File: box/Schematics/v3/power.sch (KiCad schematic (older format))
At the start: 28 parts, among them U1 AMC1100DWV, U2 ADUM5010ARSZ

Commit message: finish dsp schematics
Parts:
- added C12, C13: C, symbol C
- added U3: ISL21010CFH333Z-TK, symbol ISL21010CFH333Z-TK
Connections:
- net labels added: 3.3VREF, ADC, IN+, IN-
- net labels removed: ADC_IN+, ADC_IN-
- wire segments 97 -> 105

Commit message: create connectors sheet
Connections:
- net labels added: ADC_IN+, ADC_IN-
- net labels removed: ADC, IN+, IN-
- wire segments 105 -> 104
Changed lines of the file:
@@
 LIBS:power
 LIBS:conn
-LIBS:contrib
-LIBS:stm32
 LIBS:opqbox3-cache
 EELAYER 25 0
@@
 $Descr A4 11693 8268
 encoding utf-8
-Sheet 2 3
+Sheet 2 4
 Title ""
 Date ""
@@
 Text HLabel 1700 1950 0    60   Input ~ 0
 NEUTRAL
-Text HLabel 8500 1450 2    60   Output ~ 0
-+3.3V
-Text HLabel 5350 1350 2    60   Output ~ 0
-+5V
-Text HLabel 5350 1750 2    60   Output ~ 0
-GND
 $Comp
 L PWR_FLAG #FLG021
 U 1 1 5A83249D
-P 5200 1800
-F 0 "#FLG021" H 5200 1875 50  0001 C CNN
-F 1 "PWR_FLAG" H 5200 1950 50  0000 C CNN
-F 2 "" H 5200 1800 50  0001 C CNN
-F 3 "" H 5200 1800 50  0001 C CNN
-	1    5200 1800
+P 4900 1850
+F 0 "#FLG021" H 4900 1925 50  0001 C CNN
+F 1 "PWR_FLAG" H 4900 2000 50  0000 C CNN
+F 2 "" H 4900 1850 50  0001 C CNN
+F 3 "" H 4900 1850 50  0001 C CNN
+	1    4900 1850
 	-1   0    0    1
 $EndComp
@@
 	8400 1200 8400 1600
 Wire Wire Line
-	8200 1450 8500 1450
-Wire Wire Line
 	6800 1900 6800 2250
 Wire Wire Line
@@
 	8400 2250 8400 1900
 Connection ~ 6800 1450
-Connection ~ 8400 1450
 Wire Wire Line
 	2600 1050 2600 1500
@@
 	4300 1700 4300 1850
 Wire Wire Line
-	4900 1750 4900 1700
+	4900 1700 4900 1850
 Wire Wire Line
 	7000 1450 6800 1450
@@
 Connection ~ 4900 4200
 Connection ~ 4900 3900
-Wire Wire Line
-	4800 3900 5150 3900
-Wire Wire Line
-	4800 4200 5150 4200
 Connection ~ 5200 1350
 Wire Wire Line
@@
 Wire Notes Line
 	3600 7800 3600 500
-Wire Wire Line
-	4000 1750 5350 1750
 Connection ~ 4300 1750
 Wire Wire Line
 	4100 1350 4450 1350
-Wire Wire Line
-	4750 1350 5350 1350
 Connection ~ 4900 1750
-Connection ~ 5200 1750
-Wire Wire Line
-	5200 1800 5200 1750
 Wire Wire Line
 	5200 1350 5200 1300
@@
 	1    0    0    -1
 $EndComp
-Entry Wire Line
-	5150 3900 5250 4000
-Entry Wire Line
-	5150 4200 5250 4300
-Text Label 5050 3900 0    60   ~ 0
-IN+
-Text Label 5050 4200 0    60   ~ 0
-IN-
-Wire Bus Line
-	5250 4000 5250 4350
-Wire Bus Line
-	5250 4350 5400 4350
-Text HLabel 5400 4350 2    60   Output ~ 0
-ADC
+Text HLabel 5100 4200 2    60   Output ~ 0
+ADC_IN-
+Text HLabel 5100 3900 2    60   Output ~ 0
+ADC_IN+
+Wire Wire Line
+	4800 4200 5100 4200
+Wire Wire Line
+	4800 3900 5100 3900
+Wire Wire Line
+	4750 1350 5200 1350
+Wire Wire Line
+	4000 1750 4900 1750
+Wire Wire Line
+	8200 1450 8400 1450
+Connection ~ 8400 1450
 $EndSCHEMATC

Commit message: add component values
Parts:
- C1, C13, C2, C5, C6, C8: value C -> 0.1uF
- C10, C11: value CP -> 1uF
- C12: value C -> 1uF
- C3, C9: value C -> 10uF
- C4, C7: value CP -> 22uF
- R1: value R -> 990k
- R2: value R -> 1k
- R3, R4, R8, R9: value R -> 66.5
- R5: value R -> 30.9k
- R6, R7: value R -> 10k
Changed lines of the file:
@@
 P 6800 1750
 F 0 "C10" H 6825 1850 50  0000 L CNN
-F 1 "CP" H 6825 1650 50  0000 L CNN
+F 1 "1uF" H 6825 1650 50  0000 L CNN
 F 2 "" H 6838 1600 50  0001 C CNN
 F 3 "" H 6800 1750 50  0001 C CNN
@@
 P 8400 1750
 F 0 "C11" H 8425 1850 50  0000 L CNN
-F 1 "CP" H 8425 1650 50  0000 L CNN
+F 1 "1uF" H 8425 1650 50  0000 L CNN
 F 2 "" H 8438 1600 50  0001 C CNN
 F 3 "" H 8400 1750 50  0001 C CNN
@@
 P 4300 1550
 F 0 "C4" H 4325 1650 50  0000 L CNN
-F 1 "CP" H 4325 1450 50  0000 L CNN
+F 1 "22uF" H 4325 1450 50  0000 L CNN
 F 2 "" H 4338 1400 50  0001 C CNN
 F 3 "" H 4300 1550 50  0001 C CNN
@@
 P 4900 1550
 F 0 "C7" H 4925 1650 50  0000 L CNN
-F 1 "CP" H 4925 1450 50  0000 L CNN
+F 1 "22uF" H 4925 1450 50  0000 L CNN
 F 2 "" H 4938 1400 50  0001 C CNN
 F 3 "" H 4900 1550 50  0001 C CNN
@@
 P 2150 3600
 F 0 "R1" V 2230 3600 50  0000 C CNN
-F 1 "R" V 2150 3600 50  0000 C CNN
+F 1 "990k" V 2150 3600 50  0000 C CNN
 F 2 "" V 2080 3600 50  0001 C CNN
 F 3 "" H 2150 3600 50  0001 C CNN
@@
 P 2150 4150
 F 0 "R2" V 2230 4150 50  0000 C CNN
-F 1 "R" V 2150 4150 50  0000 C CNN
+F 1 "1k" V 2150 4150 50  0000 C CNN
 F 2 "" V 2080 4150 50  0001 C CNN
 F 3 "" H 2150 4150 50  0001 C CNN
@@
 P 2400 3900
 F 0 "R3" V 2480 3900 50  0000 C CNN
-F 1 "R" V 2400 3900 50  0000 C CNN
+F 1 "66.5" V 2400 3900 50  0000 C CNN
 F 2 "" V 2330 3900 50  0001 C CNN
 F 3 "" H 2400 3900 50  0001 C CNN
@@
 P 2400 4400
 F 0 "R4" V 2480 4400 50  0000 C CNN
-F 1 "R" V 2400 4400 50  0000 C CNN
+F 1 "66.5" V 2400 4400 50  0000 C CNN
 F 2 "" V 2330 4400 50  0001 C CNN
 F 3 "" H 2400 4400 50  0001 C CNN
@@
 P 2650 4150
 F 0 "C2" H 2675 4250 50  0000 L CNN
-F 1 "C" H 2675 4050 50  0000 L CNN
+F 1 "0.1uF" H 2675 4050 50  0000 L CNN
 F 2 "" H 2688 4000 50  0001 C CNN
 F 3 "" H 2650 4150 50  0001 C CNN
@@
 P 2650 3300
 F 0 "C1" H 2675 3400 50  0000 L CNN
-F 1 "C" H 2675 3200 50  0000 L CNN
+F 1 "0.1uF" H 2675 3200 50  0000 L CNN
 F 2 "" H 2688 3150 50  0001 C CNN
 F 3 "" H 2650 3300 50  0001 C CNN
@@
 P 3050 5550
 F 0 "C3" H 3075 5650 50  0000 L CNN
-F 1 "C" H 3075 5450 50  0000 L CNN
+F 1 "10uF" H 3075 5450 50  0000 L CNN
 F 2 "" H 3088 5400 50  0001 C CNN
 F 3 "" H 3050 5550 50  0001 C CNN
@@
 P 2400 6050
 F 0 "R5" V 2480 6050 50  0000 C CNN
-F 1 "R" V 2400 6050 50  0000 C CNN
+F 1 "30.9k" V 2400 6050 50  0000 C CNN
 F 2 "" V 2330 6050 50  0001 C CNN
 F 3 "" H 2400 6050 50  0001 C CNN
@@
 P 2400 6550
 F 0 "R6" V 2480 6550 50  0000 C CNN
-F 1 "R" V 2400 6550 50  0000 C CNN
+F 1 "10k" V 2400 6550 50  0000 C CNN
 F 2 "" V 2330 6550 50  0001 C CNN
 F 3 "" H 2400 6550 50  0001 C CNN
@@
 P 4450 6550
 F 0 "R7" V 4530 6550 50  0000 C CNN
-F 1 "R" V 4450 6550 50  0000 C CNN
+F 1 "10k" V 4450 6550 50  0000 C CNN
 F 2 "" V 4380 6550 50  0001 C CNN
 F 3 "" H 4450 6550 50  0001 C CNN
@@
 P 4750 6550
 F 0 "C6" H 4775 6650 50  0000 L CNN
-F 1 "C" H 4775 6450 50  0000 L CNN
+F 1 "0.1uF" H 4775 6450 50  0000 L CNN
 F 2 "" H 4788 6400 50  0001 C CNN
 F 3 "" H 4750 6550 50  0001 C CNN
@@
 P 5000 6550
 F 0 "C9" H 5025 6650 50  0000 L CNN
-F 1 "C" H 5025 6450 50  0000 L CNN
+F 1 "10uF" H 5025 6450 50  0000 L CNN
 F 2 "" H 5038 6400 50  0001 C CNN
 F 3 "" H 5000 6550 50  0001 C CNN
@@
 P 4900 4050
 F 0 "C8" H 4925 4150 50  0000 L CNN
-F 1 "C" H 4925 3950 50  0000 L CNN
+F 1 "0.1uF" H 4925 3950 50  0000 L CNN
 F 2 "" H 4938 3900 50  0001 C CNN
 F 3 "" H 4900 4050 50  0001 C CNN
@@
 P 4650 3900
 F 0 "R8" V 4730 3900 50  0000 C CNN
-F 1 "R" V 4650 3900 50  0000 C CNN
+F 1 "66.5" V 4650 3900 50  0000 C CNN
 F 2 "" V 4580 3900 50  0001 C CNN
 F 3 "" H 4650 3900 50  0001 C CNN
@@
 P 4650 4200
 F 0 "R9" V 4730 4200 50  0000 C CNN
-F 1 "R" V 4650 4200 50  0000 C CNN
+F 1 "66.5" V 4650 4200 50  0000 C CNN
 F 2 "" V 4580 4200 50  0001 C CNN
 F 3 "" H 4650 4200 50  0001 C CNN
@@
 P 4400 3400
 F 0 "C5" H 4425 3500 50  0000 L CNN
-F 1 "C" H 4425 3300 50  0000 L CNN
+F 1 "0.1uF" H 4425 3300 50  0000 L CNN
 F 2 "" H 4438 3250 50  0001 C CNN
 F 3 "" H 4400 3400 50  0001 C CNN
@@
 P 6850 4600
 F 0 "C12" H 6875 4700 50  0000 L CNN
-F 1 "C" H 6875 4500 50  0000 L CNN
+F 1 "1uF" H 6875 4500 50  0000 L CNN
 F 2 "" H 6888 4450 50  0001 C CNN
 F 3 "" H 6850 4600 50  0001 C CNN
@@
 P 8350 4600
 F 0 "C13" H 8375 4700 50  0000 L CNN
-F 1 "C" H 8375 4500 50  0000 L CNN
+F 1 "0.1uF" H 8375 4500 50  0000 L CNN
 F 2 "" H 8388 4450 50  0001 C CNN
 F 3 "" H 8350 4600 50  0001 C CNN

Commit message: start layout
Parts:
- removed C10, C11: 1uF, symbol CP
- removed C4, C7: 22uF, symbol CP
- removed U2: ADUM5010ARSZ, symbol ADUM5010ARSZ
- added C10, C11: 1uF, Capacitors_SMD:C_0603_HandSoldering, symbol C
- added C4, C7: 22uF, Capacitors_SMD:C_0805_HandSoldering, symbol C
- added PSU2: ADUM5010ARSZ, Housings_SSOP:SSOP-20_5.3x7.2mm_Pitch0.65mm, symbol ADUM5010ARSZ
- C1, C12, C5: footprint (none) -> Capacitors_SMD:C_0603_HandSoldering
- C13, C2, C6, C8: footprint (none) -> Capacitors_SMD:C_0402
- C3, C9: footprint (none) -> Capacitors_SMD:C_1210_HandSoldering
- F1: value Fuse -> 62mA; footprint (none) -> Fuse_Holders_and_Fuses:Fuse_SMD1206_HandSoldering
- F2: value Fuse -> 62mA; footprint (none) -> opqbox3:FUSE
- L1: value L -> 1uH; footprint (none) -> Inductors_SMD:L_Wuerth_MAPI-2512
- PSU1: footprint (none) -> opqbox3:IRM-05-5
- R1, R2: footprint (none) -> Resistors_THT:R_Axial_DIN0204_L3.6mm_D1.6mm_P5.08mm_Horizontal
- R3, R4, R8, R9: value 66.5 -> 665; footprint (none) -> Resistors_SMD:R_0402
- R5, R6, R7: footprint (none) -> Resistors_SMD:R_0402
- REG1, U3: footprint (none) -> TO_SOT_Packages_SMD:SOT-23
- RV1: footprint (none) -> Varistors:RV_Disc_D15.5_W3.9_P7.5
- U1: footprint (none) -> SMD_Packages:SOIC-8-N
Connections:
- wire segments 104 -> 110

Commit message: fix adum component
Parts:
- PSU2: footprint Housings_SSOP:SSOP-20_5.3x7.2mm_Pitch0.65mm -> (none)
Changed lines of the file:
@@
 $Comp
 L ADUM5010ARSZ PSU2
-U 1 1 5A843299
+U 1 1 5A9A0F56
 P 3050 6200
 F 0 "PSU2" H 3250 6450 60  0000 L CNN
 F 1 "ADUM5010ARSZ" H 3250 6350 60  0000 L CNN
-F 2 "Housings_SSOP:SSOP-20_5.3x7.2mm_Pitch0.65mm" H 3050 6200 60  0001 C CNN
+F 2 "" H 3050 6200 60  0001 C CNN
 F 3 "" H 3050 6200 60  0001 C CNN
 	1    3050 6200

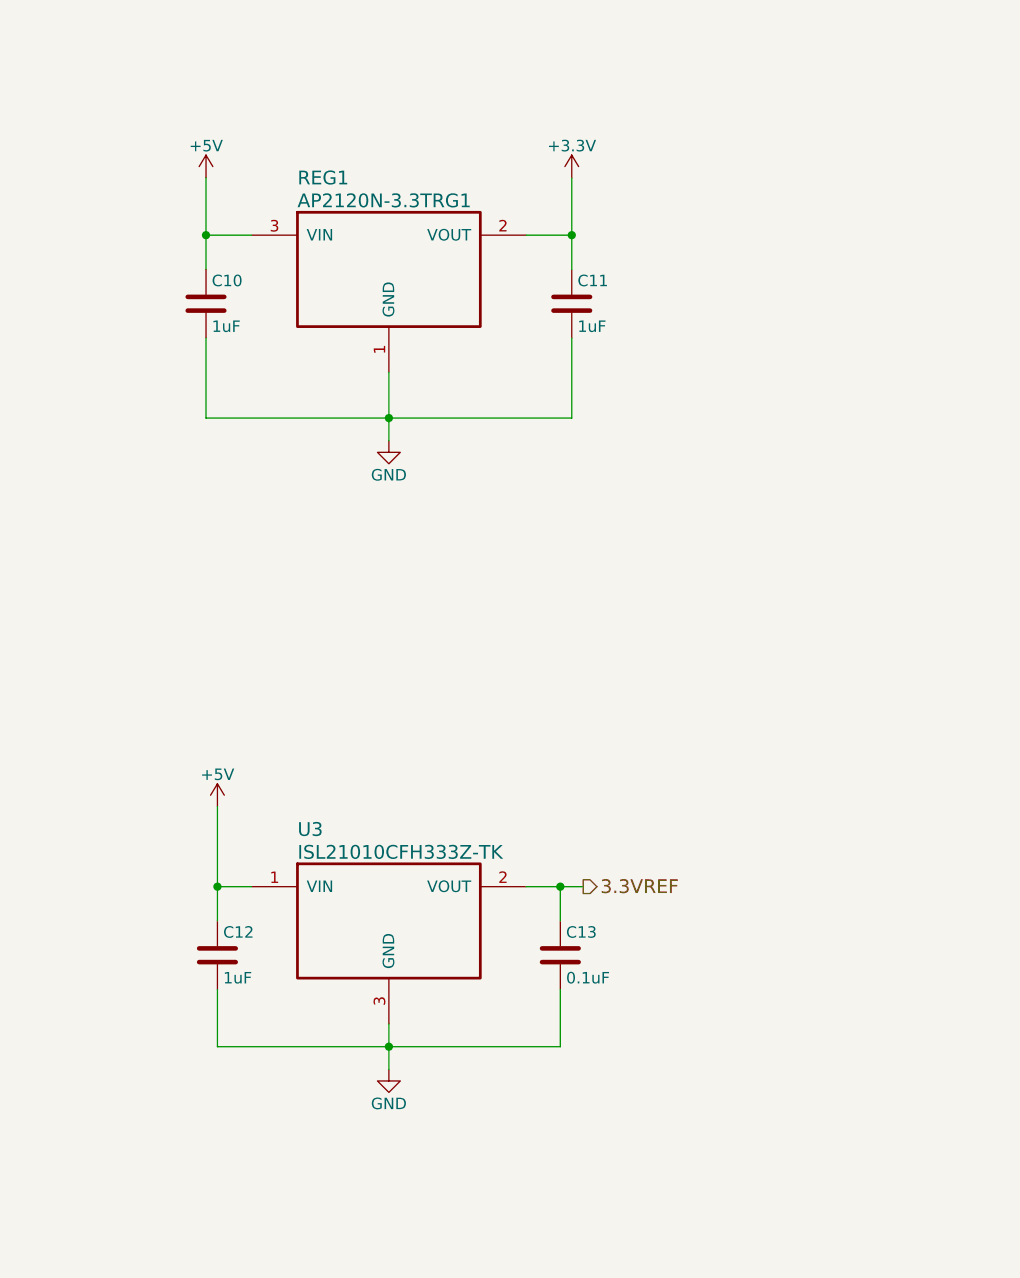
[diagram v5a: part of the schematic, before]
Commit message: add chip pro and battery
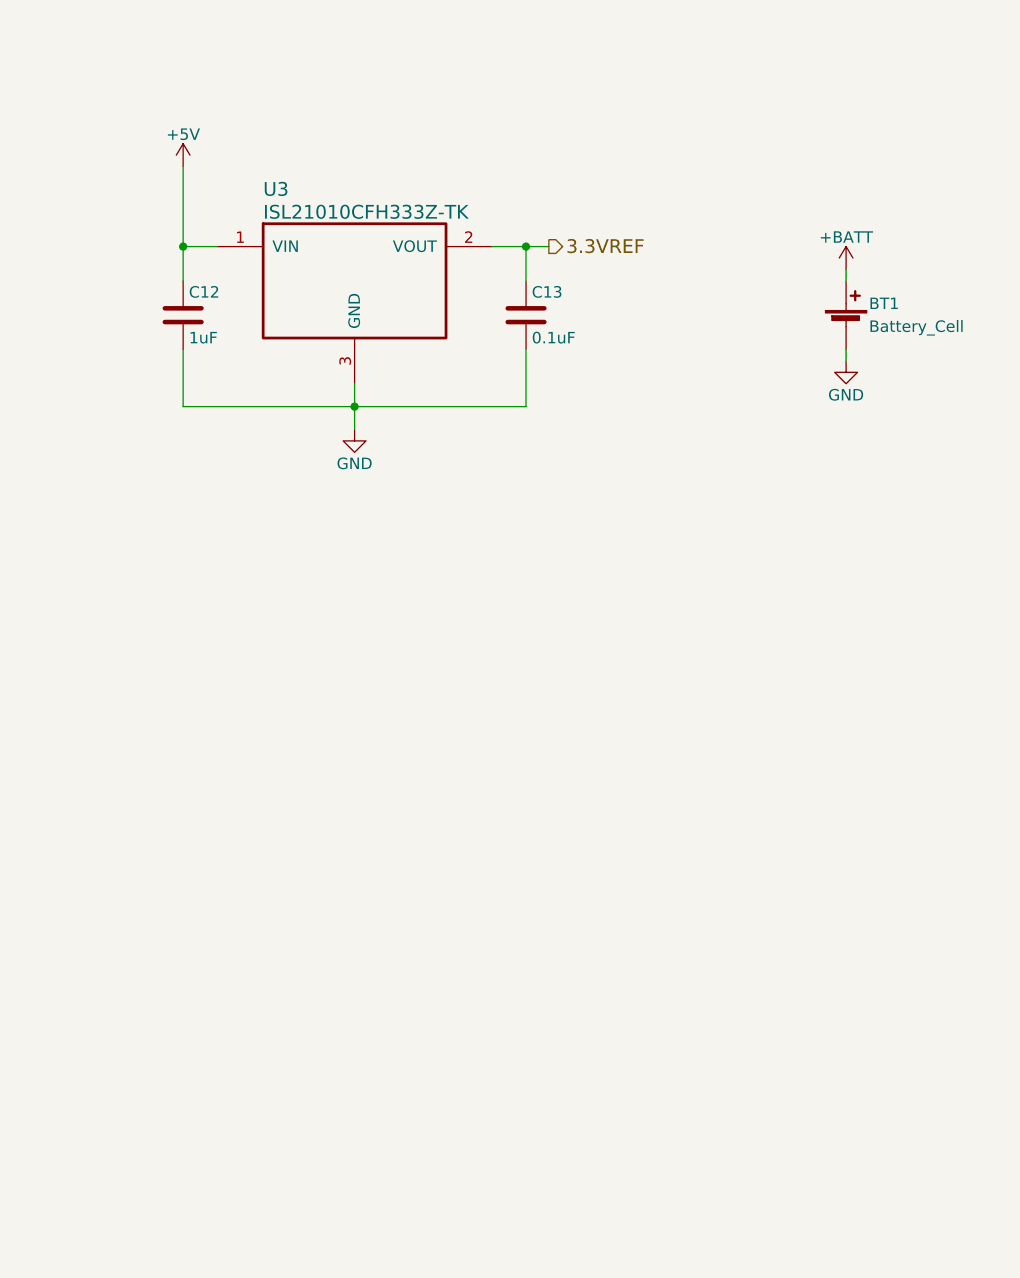
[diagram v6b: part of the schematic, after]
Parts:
- removed C10, C11: 1uF, Capacitors_SMD:C_0603_HandSoldering, symbol C
- removed REG1: AP2120N-3.3TRG1, TO_SOT_Packages_SMD:SOT-23, symbol AP2120N-3.3TRG1
- added BT1: Battery_Cell, Connectors_JST:JST_PH_B2B-PH-K_02x2.00mm_Straight, symbol Battery_Cell
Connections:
- net GND: now also BT1.2 (-)
- new net +BATT: BT1.1 (+)
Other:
- moved on the sheet: C12, C13, U3
